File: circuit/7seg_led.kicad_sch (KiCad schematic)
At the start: 26 parts, among them Q1 2SC1815, Q2 2SC1815, Q3 2SC1815, Q4 2SC1815, Q5 2SC1815, U1 OSL_40391_LRA

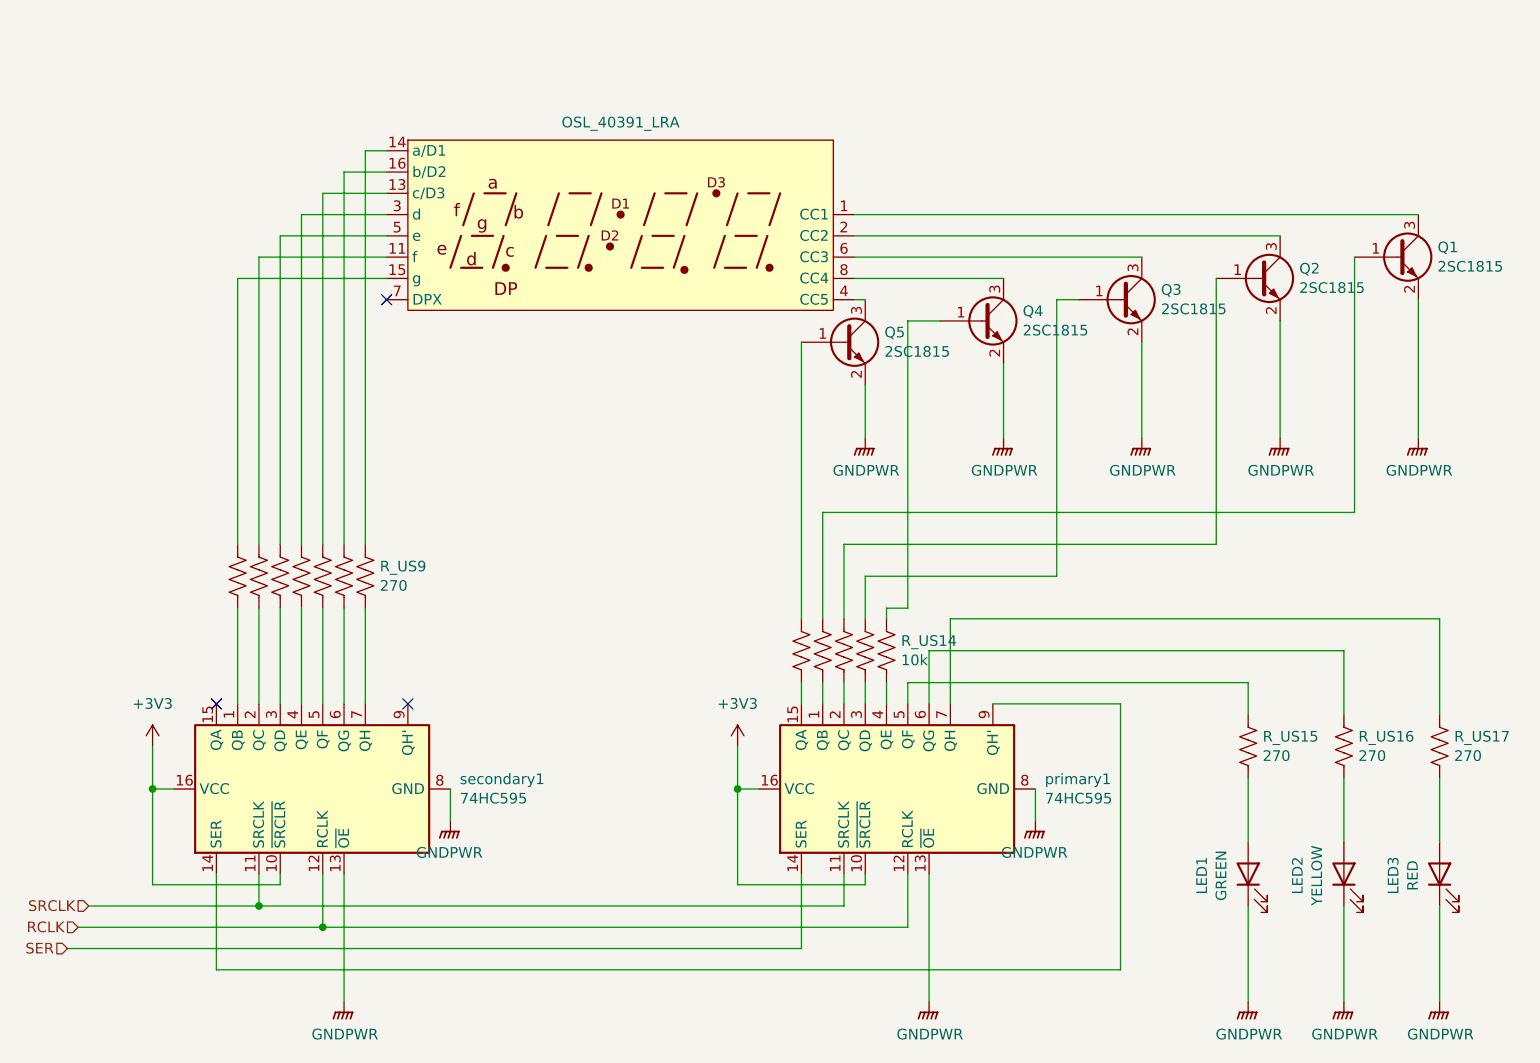
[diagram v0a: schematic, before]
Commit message: [update] update 7seg led peripheral circuit
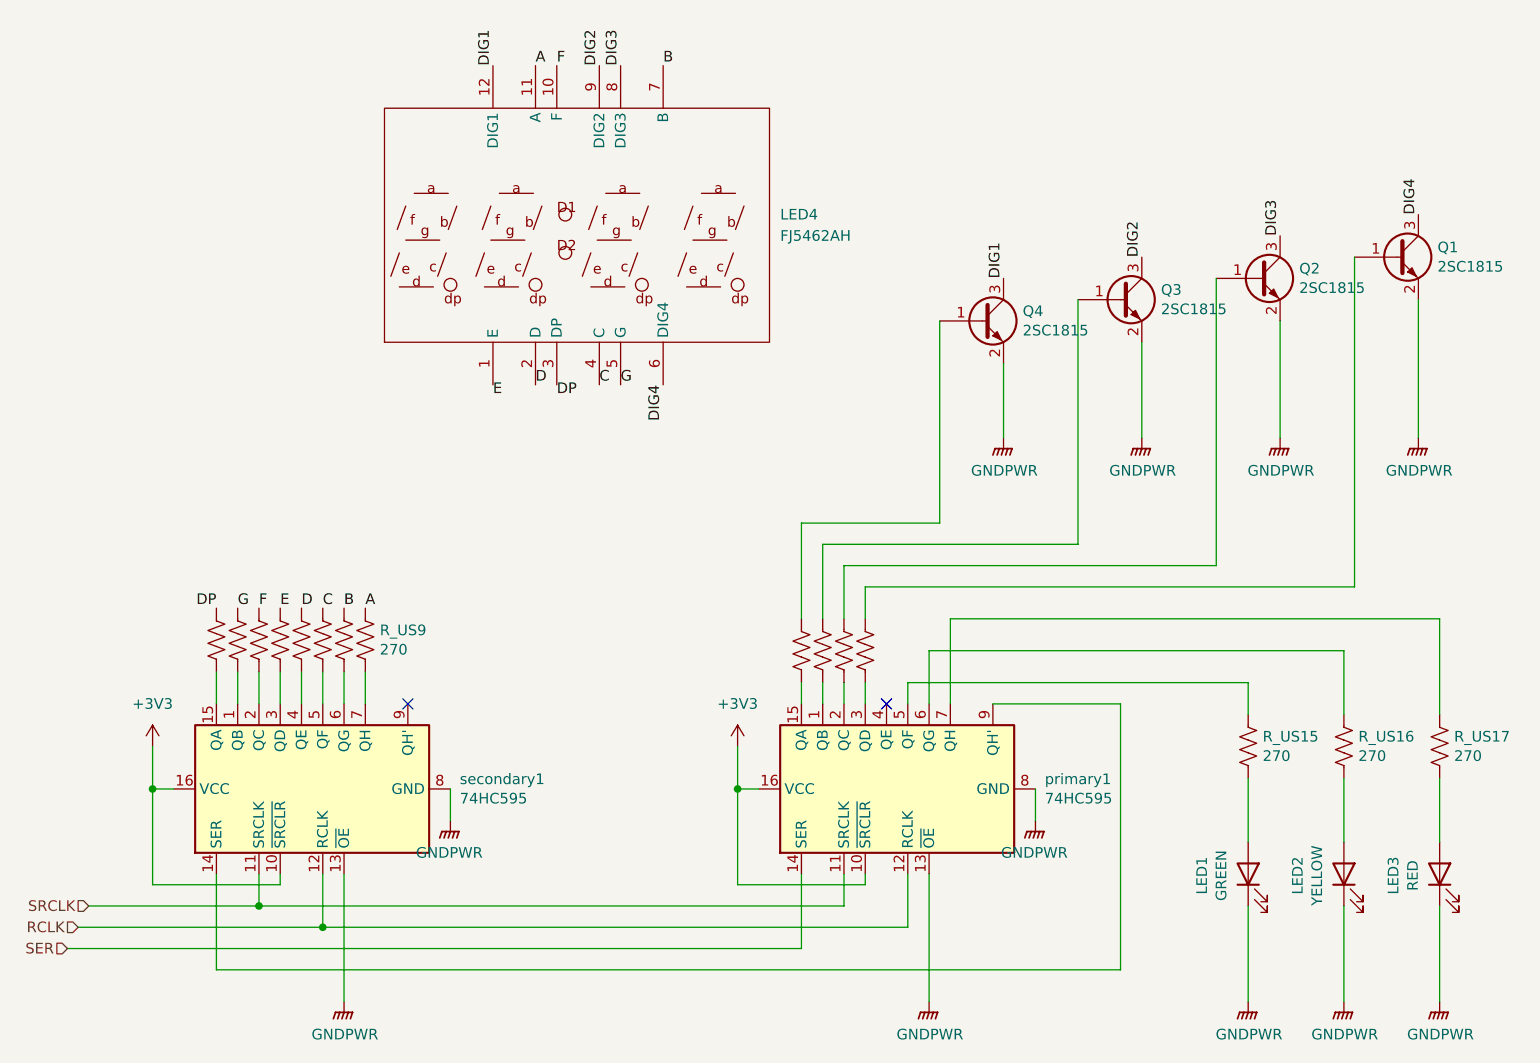
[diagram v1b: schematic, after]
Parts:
- removed Q5: 2SC1815, Package_TO_SOT_SMD:SOT-23, symbol Transistor_BJT:2SC1815
- removed R_US14: 10k, Resistor_SMD:R_0805_2012Metric, symbol Device:R_US
- removed U1: OSL_40391_LRA, MyPartsLibrary:OSL_40391_LRA, symbol control-rescue:4digit_7seg_led-Display_Character
- added LED4: FJ5462AH, FJ5462AH:LED-SEG-TH_12P-L50.3-W19.0-P2.54-S15.24-BL, symbol FJ5462AH:FJ5462AH
- added R_US19: 270, Resistor_SMD:R_0805_2012Metric, symbol Device:R_US
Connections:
- net F: now reaches R_US4.1
- net F: now also LED4.10 (F)
- net at Q4.1 (B): now also R_US10.1
- net DIG1: now reaches Q4.3 (C)
- net DIG1: now also LED4.12 (DIG1)
- net B: now reaches R_US8.1
- net B: now also LED4.7 (B)
- net at secondary1.15 (QA): now also R_US19.2
- net at R_US13.1: now also Q1.1 (B); no longer Q3.1 (B)
- net DIG3: now reaches Q2.3 (C)
- net DIG3: now also LED4.8 (DIG3)
- net DIG2: now reaches Q3.3 (C)
- net DIG2: now also LED4.9 (DIG2)
- net G: now reaches R_US3.1
- net G: now also LED4.5 (G)
- net DIG4: now reaches Q1.3 (C)
- net DIG4: now also LED4.6 (DIG4)
- net C: now reaches R_US7.1
- net C: now also LED4.4 (C)
- net A: now reaches R_US9.1
- net A: now also LED4.11 (A)
- net D: now reaches R_US6.1
- net D: now also LED4.2 (D)
- net E: now reaches R_US5.1
- net E: now also LED4.1 (E)
- net at R_US11.1: now also Q3.1 (B); no longer Q1.1 (B)
- new net DP: LED4.3 (DP), R_US19.1
- no-connect marks 3 -> 2
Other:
- moved on the sheet: R_US9

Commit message: [update] re-annotate symbols
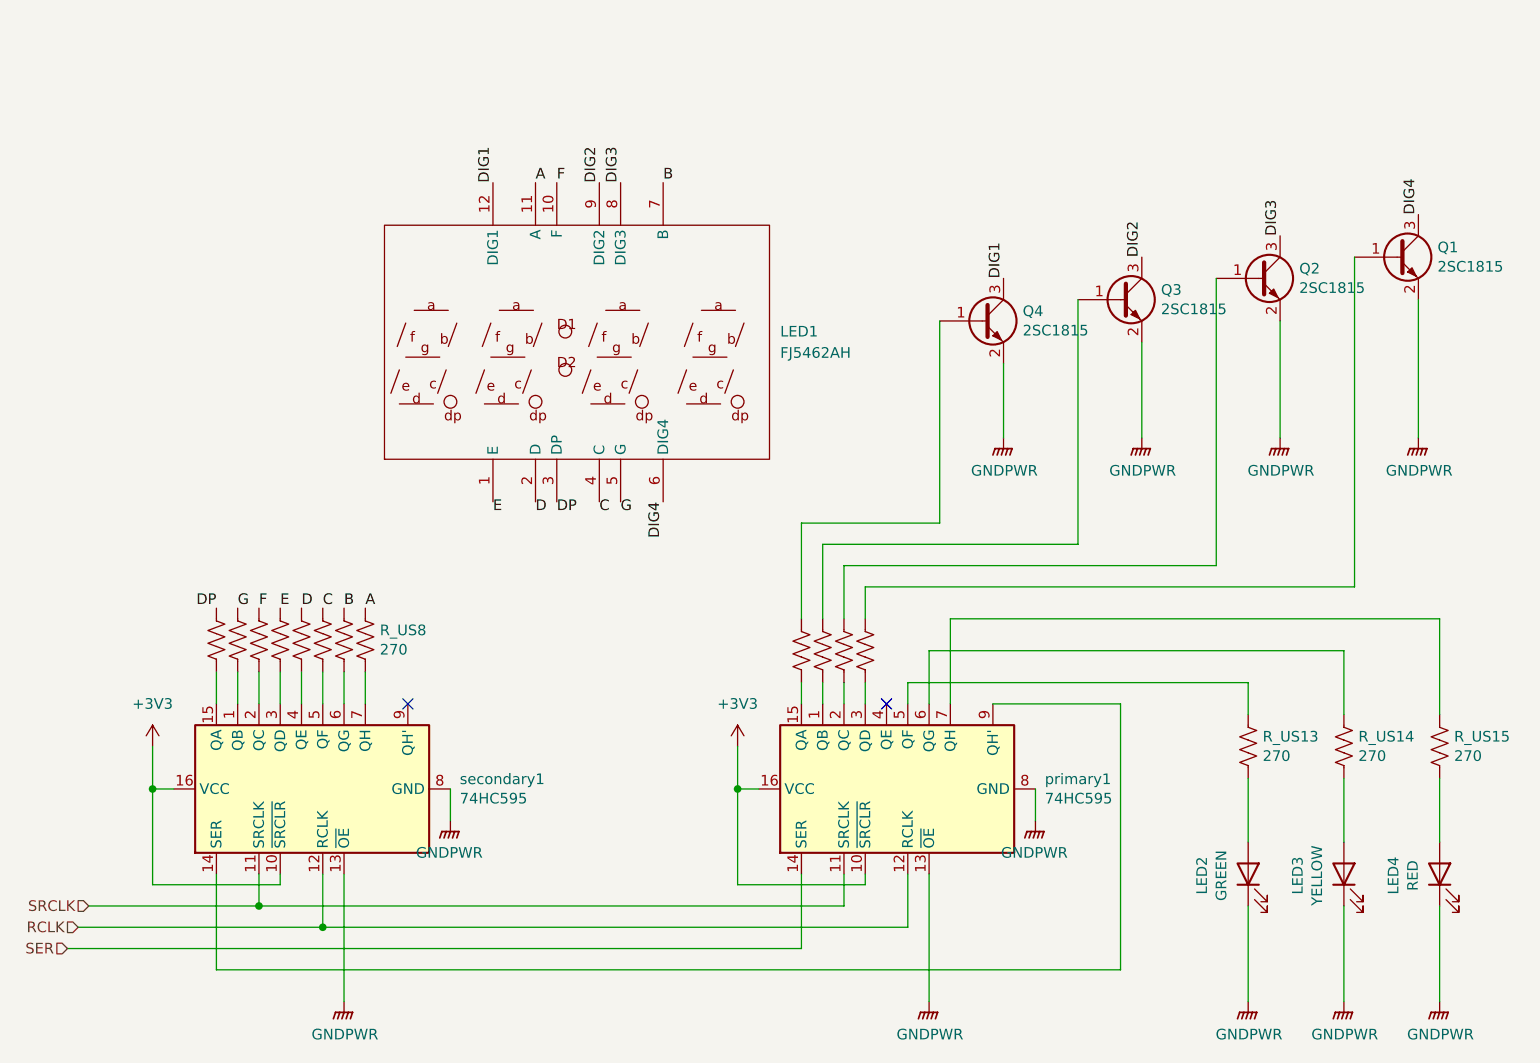
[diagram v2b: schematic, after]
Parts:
- renumbered LED4 to LED1, LED1 to LED2, LED2 to LED3, LED3 to LED4, R_US19 to R_US1, R_US11 to R_US10, R_US12 to R_US11, R_US13 to R_US12, R_US15 to R_US13, R_US16 to R_US14, R_US17 to R_US15, R_US3 to R_US2, R_US4 to R_US3, R_US5 to R_US4, R_US6 to R_US5, R_US7 to R_US6, R_US8 to R_US7, R_US9 to R_US8, R_US10 to R_US9
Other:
- moved on the sheet: LED1

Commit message: [wip][add] init pcb data
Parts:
- LED1: footprint FJ5462AH:LED-SEG-TH_12P-L50.3-W19.0-P2.54-S15.24-BL -> MyParts:FJ5462AH
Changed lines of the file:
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@@
 	(paper "A4")
+	(junction
+		(at 74.93 113.03)
+		(diameter 0)
+		(color 0 0 0 0)
+	)
 	(junction
 		(at 144.78 115.57)
@@
 	(wire
 		(pts
-			(xy 74.93 110.49) (xy 74.93 115.57)
+			(xy 74.93 113.03) (xy 74.93 115.57)
+		)
+		(stroke
+			(width 0)
+			(type default)
+		)
+	)
+	(wire
+		(pts
+			(xy 66.04 110.49) (xy 66.04 113.03)
+		)
+		(stroke
+			(width 0)
+			(type default)
+		)
+	)
+	(wire
+		(pts
+			(xy 66.04 113.03) (xy 74.93 113.03)
+		)
+		(stroke
+			(width 0)
+			(type default)
+		)
+	)
+	(wire
+		(pts
+			(xy 74.93 110.49) (xy 74.93 113.03)
 		)
 		(stroke
@@
 	(wire
 		(pts
+			(xy 144.78 110.49) (xy 144.78 115.57)
+		)
+		(stroke
+			(width 0)
+			(type default)
+		)
+	)
+	(wire
+		(pts
 			(xy 167.64 125.73) (xy 167.64 140.97)
 		)
@@
 		(pts
 			(xy 157.48 95.25) (xy 157.48 88.9)
-		)
-		(stroke
-			(width 0)
-			(type default)
-		)
-	)
-	(wire
-		(pts
-			(xy 144.78 115.57) (xy 144.78 110.49)
 		)
 		(stroke
@@
 	)
 	(symbol
+		(lib_id "power:PWR_FLAG")
+		(at 66.04 110.49 0)
+		(unit 1)
+		(exclude_from_sim no)
+		(in_bom yes)
+		(on_board yes)
+		(dnp no)
+		(fields_autoplaced yes)
+		(property "Reference" "#FLG02"
+			(at 66.04 108.585 0)
+			(effects
+				(font
+					(size 1.27 1.27)
+				)
+				(hide yes)
+			)
+		)
+		(property "Value" "PWR_FLAG"
+			(at 66.04 105.41 0)
+			(effects
+				(font
+					(size 1.27 1.27)
+				)
+			)
+		)
+		(property "Footprint" ""
+			(at 66.04 110.49 0)
+			(effects
+				(font
+					(size 1.27 1.27)
+				)
+				(hide yes)
+			)
+		)
+		(property "Datasheet" "~"
+			(at 66.04 110.49 0)
+			(effects
+				(font
+					(size 1.27 1.27)
+				)
+				(hide yes)
+			)
+		)
+		(property "Description" "Special symbol for telling ERC where power comes from"
+			(at 66.04 110.49 0)
+			(effects
+				(font
+					(size 1.27 1.27)
+				)
+				(hide yes)
+			)
+		)
+		(pin "1"
+		)
+		(instances
+			(project "gen3"
+				(path "/4fc99a72-ed0b-4d28-88d8-569af68d8cfc/5dfef49a-9007-4b14-a530-e7b7a9c1e25f"
+					(reference "#FLG02")
+					(unit 1)
+				)
+			)
+		)
+	)
+	(symbol
 		(lib_id "Device:R_US")
 		(at 92.71 97.79 0)
@@
 			)
 		)
-		(property "Footprint" "FJ5462AH:LED-SEG-TH_12P-L50.3-W19.0-P2.54-S15.24-BL"
+		(property "Footprint" "MyParts:FJ5462AH"
 			(at 125.73 62.23 0)
 			(effects

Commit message: [add] add jlcpcb bom data
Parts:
- renumbered primary1 to U1, secondary1 to U2
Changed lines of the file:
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@@
 		(on_board yes)
 		(dnp no)
-		(property "Reference" "primary1"
+		(property "Reference" "U1"
 			(at 181.4576 114.4016 90)
 			(effects
@@
 			(project "gen3"
 				(path "/4fc99a72-ed0b-4d28-88d8-569af68d8cfc/5dfef49a-9007-4b14-a530-e7b7a9c1e25f"
-					(reference "primary1")
+					(reference "U1")
 					(unit 1)
 				)
@@
 		(on_board yes)
 		(dnp no)
-		(property "Reference" "secondary1"
+		(property "Reference" "U2"
 			(at 111.6076 114.4016 90)
 			(effects
@@
 			(project "gen3"
 				(path "/4fc99a72-ed0b-4d28-88d8-569af68d8cfc/5dfef49a-9007-4b14-a530-e7b7a9c1e25f"
-					(reference "secondary1")
-					(unit 1)
-				)
+					(reference "U2")
+					(unit 1)
+				)
